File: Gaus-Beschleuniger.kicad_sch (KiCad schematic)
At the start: 8 parts, among them J7 Screw_Terminal_01x02, SW1 SW_SPDT, SW2 SW_SPDT

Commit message: rough placement
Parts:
- removed R33: 20k0, Resistor_SMD:R_0805_2012Metric_Pad1.20x1.40mm_HandSolder, symbol Device:R
- added R42: 10k, Resistor_SMD:R_0805_2012Metric_Pad1.20x1.40mm_HandSolder, symbol Device:R
- R32: value 20k0 -> 10k; MPN RC0805FR-0720KL -> RC0805FR-0710KL
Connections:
- net Controller/Discharge: now also R42.2
- net at D19.2 (A): now also R42.1
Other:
- sheet 5V Buck: file untitled.kicad_sch -> 5V_Buck.kicad_sch
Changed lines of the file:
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@@
+	)
+	(symbol
+		(lib_id "Device:R")
+		(at 101.6 77.47 180)
+		(unit 1)
+		(exclude_from_sim no)
+		(in_bom yes)
+		(on_board yes)
+		(dnp no)
+		(fields_autoplaced yes)
+		(property "Reference" "R32"
+			(at 104.14 76.1999 0)
+			(effects
+				(font
+					(size 1.27 1.27)
+				)
+				(justify right)
+			)
+		)
+		(property "Value" "10k"
+			(at 104.14 78.7399 0)
+			(effects
+				(font
+					(size 1.27 1.27)
+				)
+				(justify right)
+			)
+		)
+		(property "Footprint" "Resistor_SMD:R_0805_2012Metric_Pad1.20x1.40mm_HandSolder"
+			(at 103.378 77.47 90)
+			(effects
+				(font
+					(size 1.27 1.27)
+				)
+				(hide yes)
+			)
+		)
+		(property "Datasheet" "~"
+			(at 101.6 77.47 0)
+			(effects
+				(font
+					(size 1.27 1.27)
+				)
+				(hide yes)
+			)
+		)
+		(property "Description" "Resistor"
+			(at 101.6 77.47 0)
+			(effects
+				(font
+					(size 1.27 1.27)
+				)
+				(hide yes)
+			)
+		)
+		(property "MPN" "RC0805FR-0710KL"
+			(at 101.6 77.47 0)
+			(effects
+				(font
+					(size 1.27 1.27)
+				)
+				(hide yes)
+			)
+		)
+		(pin "2"
+		)
+		(pin "1"
+		)
+		(instances
+			(project "Gaus-Beschleuniger"
+				(path "/10afecde-cced-4b16-9a8f-ba25affe517e"
+					(reference "R32")
+					(unit 1)
+				)
+			)
+		)
 	)
 	(symbol
@@
 	)
 	(symbol
-		(lib_id "Device:R")
-		(at 110.49 77.47 180)
-		(unit 1)
-		(exclude_from_sim no)
-		(in_bom yes)
-		(on_board yes)
-		(dnp no)
-		(property "Reference" "R33"
-			(at 107.95 77.47 90)
-			(effects
-				(font
-					(size 1.27 1.27)
-				)
-			)
-		)
-		(property "Value" "20k0"
-			(at 113.03 77.47 90)
-			(effects
-				(font
-					(size 1.27 1.27)
-				)
-			)
-		)
-		(property "Footprint" "Resistor_SMD:R_0805_2012Metric_Pad1.20x1.40mm_HandSolder"
-			(at 112.268 77.47 90)
-			(effects
-				(font
-					(size 1.27 1.27)
-				)
-				(hide yes)
-			)
-		)
-		(property "Datasheet" "~"
-			(at 110.49 77.47 0)
-			(effects
-				(font
-					(size 1.27 1.27)
-				)
-				(hide yes)
-			)
-		)
-		(property "Description" "Resistor"
-			(at 110.49 77.47 0)
-			(effects
-				(font
-					(size 1.27 1.27)
-				)
-				(hide yes)
-			)
-		)
-		(property "MPN" "RC0805FR-0720KL"
-			(at 110.49 77.47 0)
-			(effects
-				(font
-					(size 1.27 1.27)
-				)
-				(hide yes)
-			)
-		)
-		(pin "1"
-		)
-		(pin "2"
-		)
-		(instances
-			(project "Gaus-Beschleuniger"
-				(path "/10afecde-cced-4b16-9a8f-ba25affe517e"
-					(reference "R33")
-					(unit 1)
-				)
-			)
-		)
-	)
-	(symbol
 		(lib_id "power:+5V")
 		(at 95.25 22.86 0)
@@
 	(symbol
 		(lib_id "Device:R")
-		(at 101.6 77.47 180)
-		(unit 1)
-		(exclude_from_sim no)
-		(in_bom yes)
-		(on_board yes)
-		(dnp no)
-		(property "Reference" "R32"
-			(at 99.06 77.47 90)
-			(effects
-				(font
-					(size 1.27 1.27)
-				)
-			)
-		)
-		(property "Value" "20k0"
-			(at 104.14 77.47 90)
-			(effects
-				(font
-					(size 1.27 1.27)
-				)
+		(at 110.49 77.47 180)
+		(unit 1)
+		(exclude_from_sim no)
+		(in_bom yes)
+		(on_board yes)
+		(dnp no)
+		(fields_autoplaced yes)
+		(property "Reference" "R42"
+			(at 113.03 76.1999 0)
+			(effects
+				(font
+					(size 1.27 1.27)
+				)
+				(justify right)
+			)
+		)
+		(property "Value" "10k"
+			(at 113.03 78.7399 0)
+			(effects
+				(font
+					(size 1.27 1.27)
+				)
+				(justify right)
 			)
 		)
 		(property "Footprint" "Resistor_SMD:R_0805_2012Metric_Pad1.20x1.40mm_HandSolder"
-			(at 103.378 77.47 90)
+			(at 112.268 77.47 90)
 			(effects
 				(font
@@
 		)
 		(property "Datasheet" "~"
-			(at 101.6 77.47 0)
+			(at 110.49 77.47 0)
 			(effects
 				(font
@@
 		)
 		(property "Description" "Resistor"
-			(at 101.6 77.47 0)
-			(effects
-				(font
-					(size 1.27 1.27)
-				)
-				(hide yes)
-			)
-		)
-		(property "MPN" "RC0805FR-0720KL"
-			(at 101.6 77.47 0)
-			(effects
-				(font
-					(size 1.27 1.27)
-				)
-				(hide yes)
-			)
-		)
-		(pin "1"
+			(at 110.49 77.47 0)
+			(effects
+				(font
+					(size 1.27 1.27)
+				)
+				(hide yes)
+			)
+		)
+		(property "MPN" "RC0805FR-0710KL"
+			(at 110.49 77.47 0)
+			(effects
+				(font
+					(size 1.27 1.27)
+				)
+				(hide yes)
+			)
 		)
 		(pin "2"
 		)
+		(pin "1"
+		)
 		(instances
 			(project "Gaus-Beschleuniger"
 				(path "/10afecde-cced-4b16-9a8f-ba25affe517e"
-					(reference "R32")
+					(reference "R42")
 					(unit 1)
 				)
@@
 			)
 		)
-		(property "Sheetfile" "untitled.kicad_sch"
+		(property "Sheetfile" "5V_Buck.kicad_sch"
 			(at 80.01 41.2246 0)
 			(effects

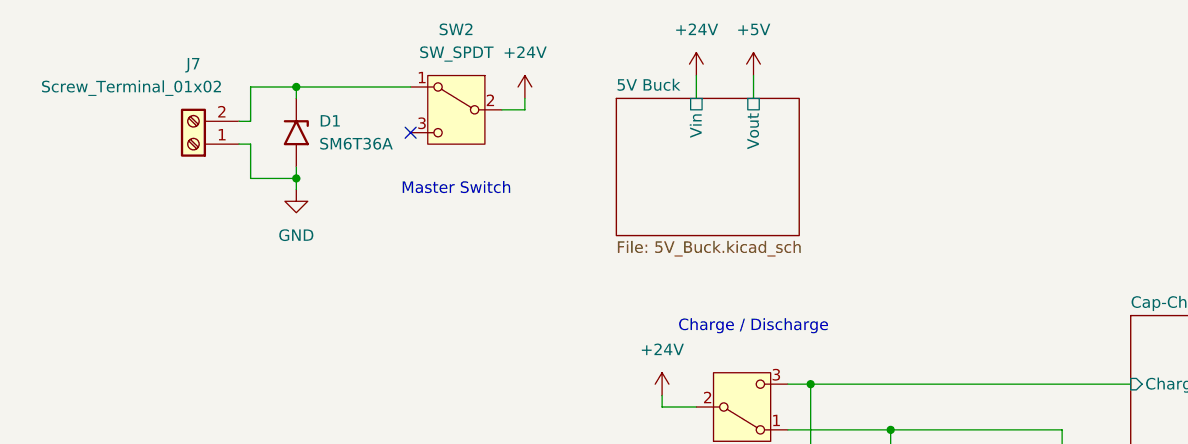
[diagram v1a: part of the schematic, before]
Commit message: placement and routing done drc errors, stiching vias and polish next
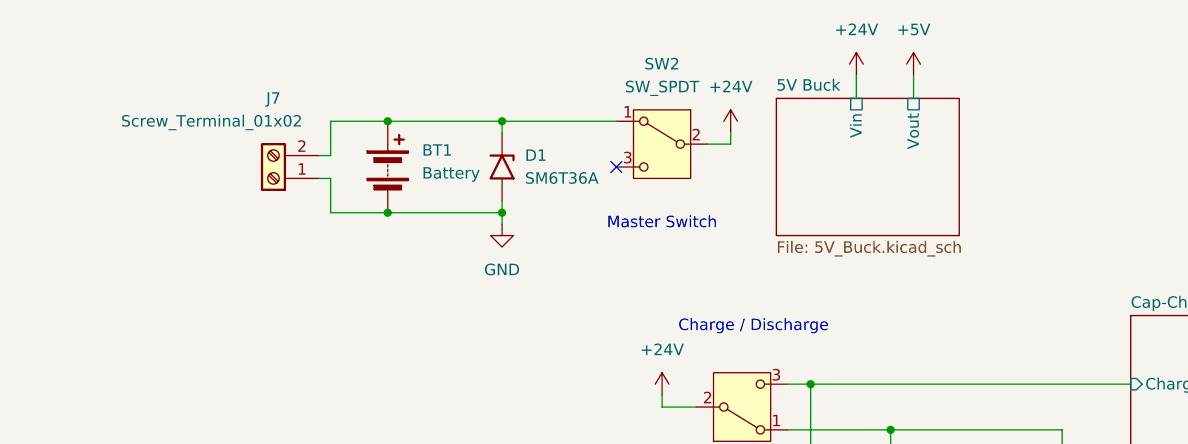
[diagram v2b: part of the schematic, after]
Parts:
- added BT1: Battery, Connector_AMASS:AMASS_XT60-M_1x02_P7.20mm_Vertical, symbol Device:Battery
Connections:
- net GND: now also BT1.2 (-)
- net at D1.1 (A1), J7.2 (Pin_2), SW2.1 (A): now also BT1.1 (+)
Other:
- moved on the sheet: D1, J7, SW2

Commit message: Layout finished
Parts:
- added H1, H2, H3, H4: MountingHole, MountingHole:MountingHole_4.3mm_M4_DIN965, symbol Mechanical:MountingHole
- added H5, H6, H7, H8: MountingHole, MountingHole:MountingHole_3.2mm_M3_DIN965, symbol Mechanical:MountingHole
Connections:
- net GND: now also J7.2 (Pin_2); no longer J7.1 (Pin_1)
- net at BT1.1 (+), D1.1 (A1), SW2.1 (A): now also J7.1 (Pin_1); no longer J7.2 (Pin_2)
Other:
- note added: "Barrel- carrier"
- note added: "Board- Standoffs"
- moved on the sheet: J7

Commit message: update fab files ;/
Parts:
- BT1: LCSC_Part_# (none) -> C5334533
- D1: LCSC_Part_# (none) -> C7436537
- J7: now not fitted
- R32, R42: LCSC_Part_# (none) -> C84376
- SW1, SW2: LCSC_Part_# (none) -> C4950128
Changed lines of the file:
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@@
+			)
+		)
+		(property "LCSC_Part_#" ""
+			(at 20.32 60.96 0)
+			(effects
+				(font
+					(size 1.27 1.27)
+				)
+				(hide yes)
 			)
 		)
@@
 			)
 		)
+		(property "LCSC_Part_#" "C84376"
+			(at 101.6 77.47 0)
+			(effects
+				(font
+					(size 1.27 1.27)
+				)
+				(hide yes)
+			)
+		)
 		(pin "2"
 		)
@@
 			)
 		)
+		(property "LCSC_Part_#" ""
+			(at 39.37 55.88 0)
+			(effects
+				(font
+					(size 1.27 1.27)
+				)
+				(hide yes)
+			)
+		)
 		(instances
 			(project "Gaus-Beschleuniger"
@@
 			)
 		)
+		(property "LCSC_Part_#" ""
+			(at 39.37 50.8 0)
+			(effects
+				(font
+					(size 1.27 1.27)
+				)
+				(hide yes)
+			)
+		)
 		(instances
 			(project "Gaus-Beschleuniger"
@@
 		(in_bom yes)
 		(on_board yes)
-		(dnp no)
+		(dnp yes)
 		(property "Reference" "J7"
 			(at 41.91 29.21 0)
@@
 		)
 		(property "Description" "Generic screw terminal, single row, 01x02, script generated (kicad-library-utils/schlib/autogen/connector/)"
+			(at 41.91 31.75 0)
+			(effects
+				(font
+					(size 1.27 1.27)
+				)
+				(hide yes)
+			)
+		)
+		(property "LCSC_Part_#" ""
 			(at 41.91 31.75 0)
 			(effects
@@
 			)
 		)
+		(property "LCSC_Part_#" ""
+			(at 39.37 60.96 0)
+			(effects
+				(font
+					(size 1.27 1.27)
+				)
+				(hide yes)
+			)
+		)
 		(instances
 			(project "Gaus-Beschleuniger"
@@
 			)
 		)
+		(property "LCSC_Part_#" "C5334533"
+			(at 54.61 33.02 0)
+			(effects
+				(font
+					(size 1.27 1.27)
+				)
+				(hide yes)
+			)
+		)
 		(pin "2"
 		)
@@
 			)
 		)
+		(property "LCSC_Part_#" ""
+			(at 20.32 55.88 0)
+			(effects
+				(font
+					(size 1.27 1.27)
+				)
+				(hide yes)
+			)
+		)
 		(instances
 			(project "Gaus-Beschleuniger"
@@
 			)
 		)
+		(property "LCSC_Part_#" ""
+			(at 110.49 86.36 0)
+			(effects
+				(font
+					(size 1.27 1.27)
+				)
+				(hide yes)
+			)
+		)
 		(pin "1"
 		)
@@
 			)
 		)
+		(property "LCSC_Part_#" "C7436537"
+			(at 67.31 33.02 90)
+			(effects
+				(font
+					(size 1.27 1.27)
+				)
+				(hide yes)
+			)
+		)
 		(pin "2"
 		)
@@
 			)
 		)
+		(property "LCSC_Part_#" "C4950128"
+			(at 93.98 59.69 0)
+			(effects
+				(font
+					(size 1.27 1.27)
+				)
+				(hide yes)
+			)
+		)
 		(pin "3"
 		)
@@
 			)
 		)
+		(property "LCSC_Part_#" ""
+			(at 39.37 66.04 0)
+			(effects
+				(font
+					(size 1.27 1.27)
+				)
+				(hide yes)
+			)
+		)
 		(instances
 			(project "Gaus-Beschleuniger"
@@
 			)
 		)
+		(property "LCSC_Part_#" ""
+			(at 20.32 50.8 0)
+			(effects
+				(font
+					(size 1.27 1.27)
+				)
+				(hide yes)
+			)
+		)
 		(instances
 			(project ""
@@
 			)
 		)
+		(property "LCSC_Part_#" ""
+			(at 20.32 66.04 0)
+			(effects
+				(font
+					(size 1.27 1.27)
+				)
+				(hide yes)
+			)
+		)
 		(instances
 			(project "Gaus-Beschleuniger"
@@
 			)
 		)
+		(property "LCSC_Part_#" "C84376"
+			(at 110.49 77.47 0)
+			(effects
+				(font
+					(size 1.27 1.27)
+				)
+				(hide yes)
+			)
+		)
 		(pin "2"
 		)
@@
 			)
 		)
+		(property "LCSC_Part_#" "C4950128"
+			(at 85.09 30.48 0)
+			(effects
+				(font
+					(size 1.27 1.27)
+				)
+				(hide yes)
+			)
+		)
 		(pin "3"
 		)
@@
 			(effects
 				(font
+					(size 1.27 1.27)
+				)
+				(hide yes)
+			)
+		)
+		(property "LCSC_Part_#" ""
+			(at 101.6 86.36 0)
+			(effects
+				(font
